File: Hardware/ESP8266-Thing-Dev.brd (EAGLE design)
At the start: 55.4 x 33.8 mm, 84 parts, among them J1 DNP, Q1 MMBT2222A, Q2 MMBT2222A, Q4 BSS138, Q5 BSS138, Q6 BSS138, Q7 BSS138, Q8 BSS138, U1 AP2112K-3.3V, U2 ESP8266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

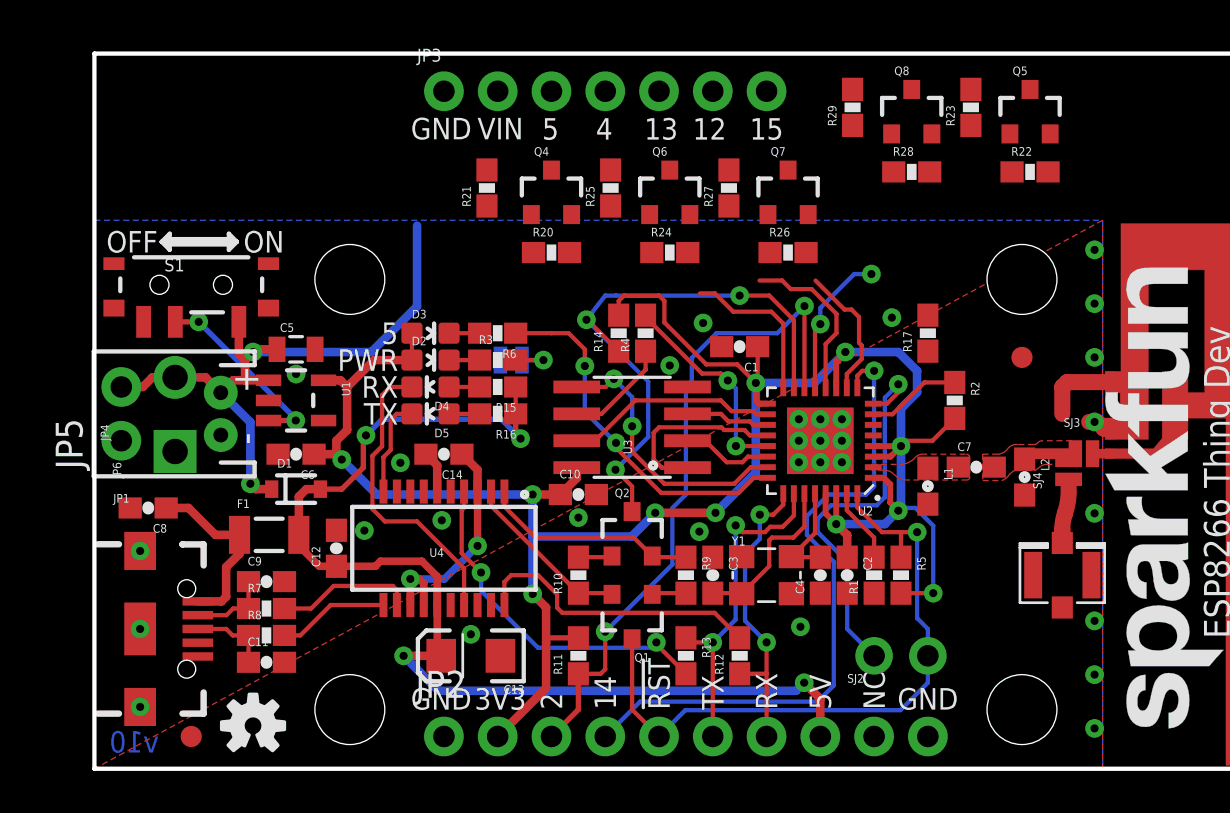
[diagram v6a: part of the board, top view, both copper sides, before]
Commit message: Route level shifter nets and start cleaning up DRC warnings.
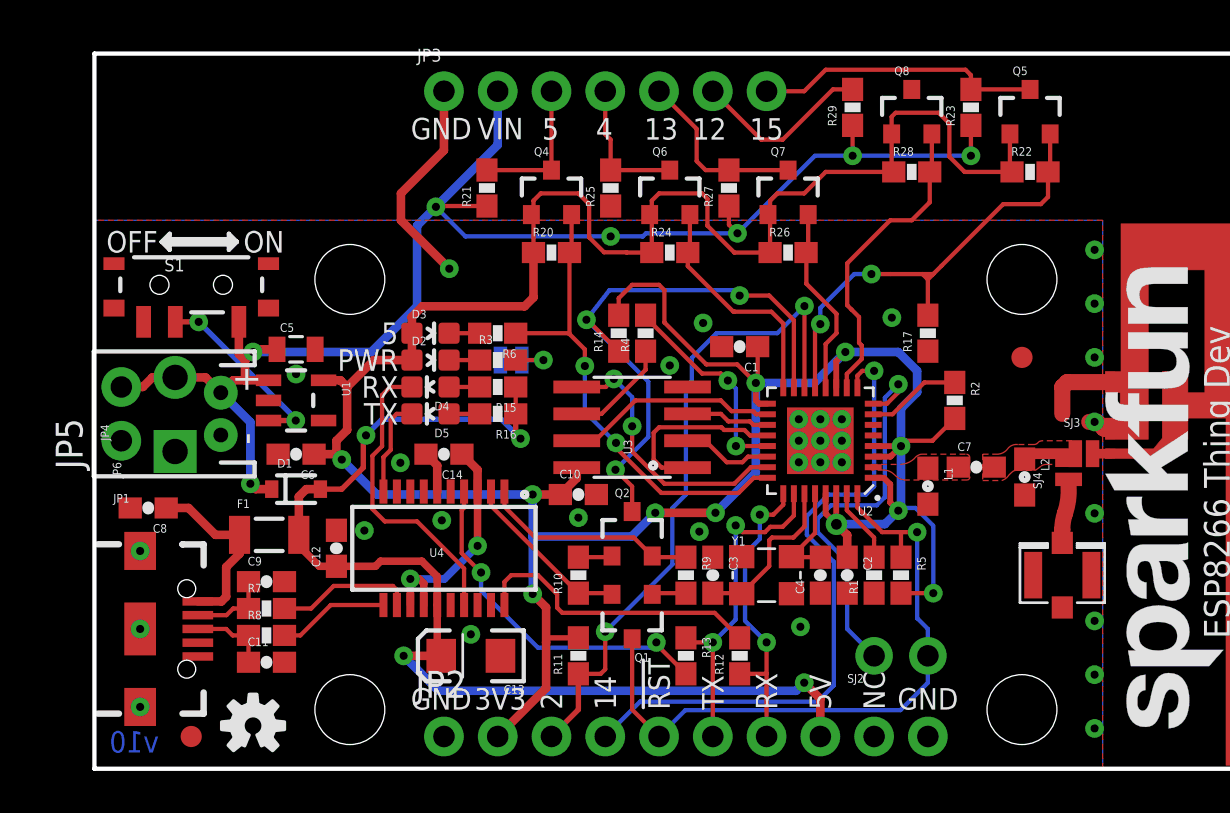
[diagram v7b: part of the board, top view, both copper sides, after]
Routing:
- net VCC: track 107.2 -> 158.7 mm
- net VIN: track 30.7 -> 72.9 mm, vias 2 -> 7
- net GPIO15: track 7.08 -> 22.2 mm
- net GPIO15_OUT: track 0.00 -> 13.6 mm
- net GND: track 6.74 -> 16.9 mm, vias 31 -> 32
- net GPIO13_OUT: track 0.00 -> 8.54 mm
- net GPIO12_OUT: track 0.00 -> 8.53 mm
- net GPIO12: track 6.46 -> 14.8 mm
- net GPIO5_OUT: track 0.00 -> 6.78 mm
- net GPIO4_OUT: track 0.00 -> 6.62 mm
- net GPIO5: track 17.2 -> 22.9 mm
- net GPIO4: track 7.56 -> 11.2 mm
- net GPIO13: track 7.99 -> 9.09 mm
